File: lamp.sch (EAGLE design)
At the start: 15 parts, among them IC1 LM358D, T2 TIP32C

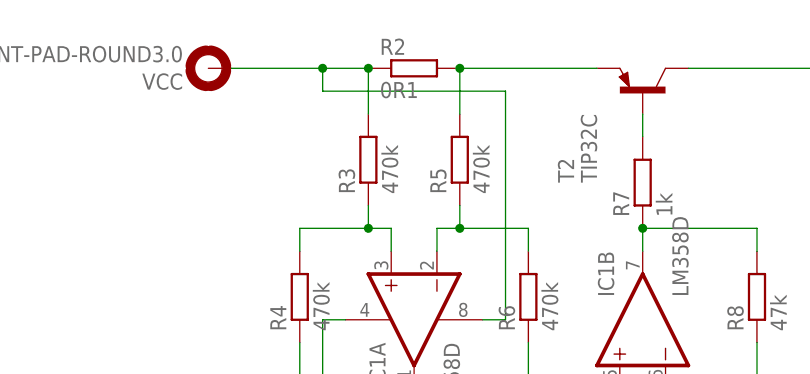
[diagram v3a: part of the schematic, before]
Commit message: Adjusted resistor values & packages.
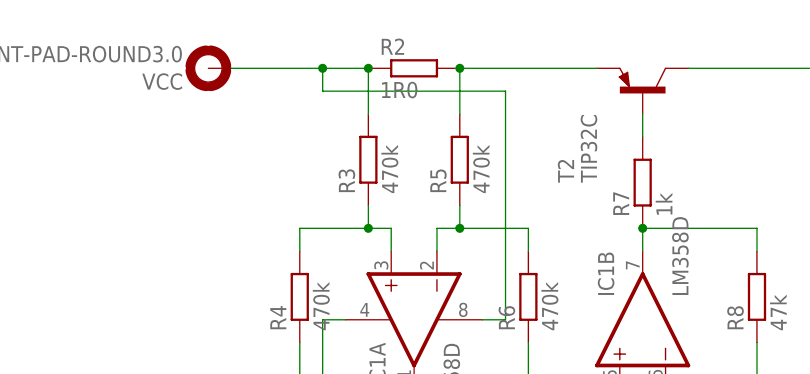
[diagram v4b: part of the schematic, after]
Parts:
- R2: value 0R1 -> 1R0; device resistor:R-EU_0617/17 -> resistor:R-EU_R1210
- R3, R4, R5, R6, R7, R8: device resistor:R-EU_M1206 -> resistor:R-EU_R1206
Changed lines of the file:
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@@
 <part name="IC1" library="linear" deviceset="LM358" device="D" value="LM358D"/>
 <part name="R1" library="pot" deviceset="TRIM_EU-" device="RJ9W" value="10k"/>
-<part name="R2" library="resistor" deviceset="R-EU_" device="0617/17" value="0R1"/>
-<part name="R3" library="resistor" deviceset="R-EU_" device="M1206" value="470k"/>
-<part name="R4" library="resistor" deviceset="R-EU_" device="M1206" value="470k"/>
-<part name="R5" library="resistor" deviceset="R-EU_" device="M1206" value="470k"/>
-<part name="R6" library="resistor" deviceset="R-EU_" device="M1206" value="470k"/>
+<part name="R2" library="resistor" deviceset="R-EU_" device="R1210" value="1R0"/>
+<part name="R3" library="resistor" deviceset="R-EU_" device="R1206" value="470k"/>
+<part name="R4" library="resistor" deviceset="R-EU_" device="R1206" value="470k"/>
+<part name="R5" library="resistor" deviceset="R-EU_" device="R1206" value="470k"/>
+<part name="R6" library="resistor" deviceset="R-EU_" device="R1206" value="470k"/>
 <part name="LED2" library="led" deviceset="Z-POWER-LED" device=""/>
 <part name="LED3" library="led" deviceset="Z-POWER-LED" device=""/>
-<part name="R7" library="resistor" deviceset="R-EU_" device="M1206" value="1k"/>
+<part name="R7" library="resistor" deviceset="R-EU_" device="R1206" value="1k"/>
 <part name="T2" library="transistor" deviceset="TIP32" device="" technology="C"/>
-<part name="R8" library="resistor" deviceset="R-EU_" device="M1206" value="47k"/>
+<part name="R8" library="resistor" deviceset="R-EU_" device="R1206" value="47k"/>
 <part name="VCC" library="holes" deviceset="MOUNT-PAD-ROUND" device="3.0"/>
 <part name="GND" library="holes" deviceset="MOUNT-PAD-ROUND" device="3.0"/>

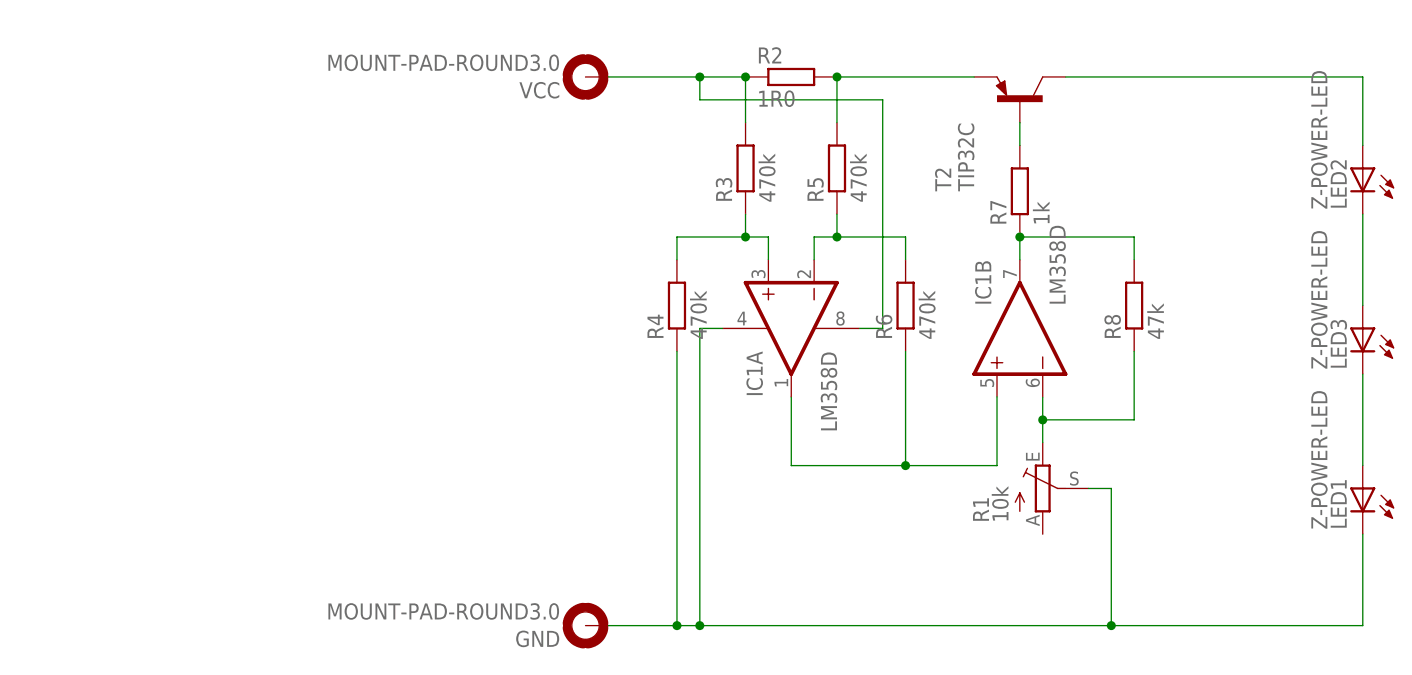
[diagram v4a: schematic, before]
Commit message: Added a power switch.
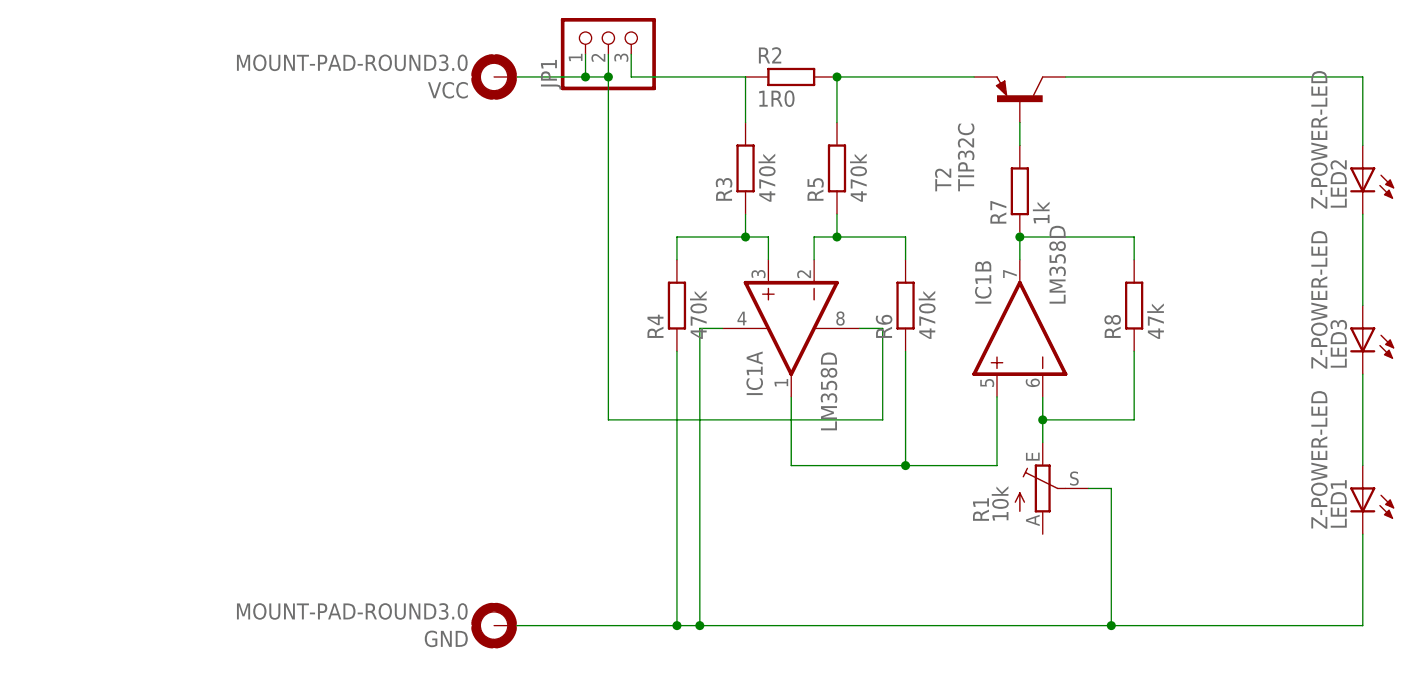
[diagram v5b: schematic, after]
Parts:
- added JP1: (no value), pinhead:PINHD-1X3
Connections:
- new net N$24: JP1.3, R2.1, R3.2
- net VCC: now also JP1.1, JP1.2; no longer R2.1, R3.2
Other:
- moved on the sheet: GND, VCC
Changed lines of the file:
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@@
 <part name="VCC" library="holes" deviceset="MOUNT-PAD-ROUND" device="3.0"/>
 <part name="GND" library="holes" deviceset="MOUNT-PAD-ROUND" device="3.0"/>
+<part name="JP1" library="pinhead" deviceset="PINHD-1X3" device=""/>
 </parts>
 <sheets>
@@
 <instance part="T2" gate="G$1" x="43.18" y="91.44" rot="R90"/>
 <instance part="R8" gate="G$1" x="55.88" y="68.58" rot="R90"/>
-<instance part="VCC" gate="G$1" x="-5.08" y="93.98" rot="R180"/>
-<instance part="GND" gate="G$1" x="-5.08" y="33.02" rot="R180"/>
+<instance part="VCC" gate="G$1" x="-15.24" y="93.98" rot="R180"/>
+<instance part="GND" gate="G$1" x="-15.24" y="33.02" rot="R180"/>
 <instance part="IC1" gate="P" x="17.78" y="66.04" rot="MR90"/>
+<instance part="JP1" gate="A" x="-2.54" y="99.06" rot="R90"/>
 </instances>
 <busses>
 </busses>
 <nets>
-<net name="VCC" class="0">
-<segment>
-<wire x1="-2.54" y1="93.98" x2="7.62" y2="93.98" width="0.1524" layer="91"/>
-<pinref part="R2" gate="G$1" pin="1"/>
-<pinref part="VCC" gate="G$1" pin="MOUNT"/>
-<pinref part="R3" gate="G$1" pin="2"/>
-<wire x1="7.62" y1="93.98" x2="12.7" y2="93.98" width="0.1524" layer="91"/>
-<wire x1="12.7" y1="93.98" x2="12.7" y2="88.9" width="0.1524" layer="91"/>
-<junction x="12.7" y="93.98"/>
-<pinref part="IC1" gate="P" pin="V+"/>
-<wire x1="25.4" y1="66.04" x2="27.94" y2="66.04" width="0.1524" layer="91"/>
-<wire x1="27.94" y1="66.04" x2="27.94" y2="91.44" width="0.1524" layer="91"/>
-<wire x1="27.94" y1="91.44" x2="7.62" y2="91.44" width="0.1524" layer="91"/>
-<wire x1="7.62" y1="91.44" x2="7.62" y2="93.98" width="0.1524" layer="91"/>
-<junction x="7.62" y="93.98"/>
-</segment>
-</net>
 <net name="N$2" class="0">
 <segment>
@@
 <wire x1="53.34" y1="33.02" x2="7.62" y2="33.02" width="0.1524" layer="91"/>
 <wire x1="7.62" y1="33.02" x2="5.08" y2="33.02" width="0.1524" layer="91"/>
-<wire x1="5.08" y1="33.02" x2="-2.54" y2="33.02" width="0.1524" layer="91"/>
+<wire x1="5.08" y1="33.02" x2="-12.7" y2="33.02" width="0.1524" layer="91"/>
 <wire x1="50.8" y1="48.26" x2="53.34" y2="48.26" width="0.1524" layer="91"/>
 <wire x1="53.34" y1="48.26" x2="53.34" y2="33.02" width="0.1524" layer="91"/>
@@
 </segment>
 </net>
+<net name="VCC" class="0">
+<segment>
+<pinref part="JP1" gate="A" pin="1"/>
+<wire x1="-12.7" y1="93.98" x2="-5.08" y2="93.98" width="0.1524" layer="91"/>
+<wire x1="-5.08" y1="96.52" x2="-5.08" y2="93.98" width="0.1524" layer="91"/>
+<pinref part="JP1" gate="A" pin="2"/>
+<wire x1="-5.08" y1="93.98" x2="-2.54" y2="93.98" width="0.1524" layer="91"/>
+<wire x1="-2.54" y1="93.98" x2="-2.54" y2="96.52" width="0.1524" layer="91"/>
+<junction x="-5.08" y="93.98"/>
+<pinref part="VCC" gate="G$1" pin="MOUNT"/>
+<pinref part="IC1" gate="P" pin="V+"/>
+<wire x1="25.4" y1="66.04" x2="27.94" y2="66.04" width="0.1524" layer="91"/>
+<wire x1="27.94" y1="66.04" x2="27.94" y2="55.88" width="0.1524" layer="91"/>
+<wire x1="27.94" y1="55.88" x2="-2.54" y2="55.88" width="0.1524" layer="91"/>
+<wire x1="-2.54" y1="55.88" x2="-2.54" y2="93.98" width="0.1524" layer="91"/>
+<junction x="-2.54" y="93.98"/>
+</segment>
+</net>
+<net name="N$24" class="0">
+<segment>
+<pinref part="R3" gate="G$1" pin="2"/>
+<pinref part="R2" gate="G$1" pin="1"/>
+<wire x1="12.7" y1="93.98" x2="12.7" y2="88.9" width="0.1524" layer="91"/>
+<pinref part="JP1" gate="A" pin="3"/>
+<wire x1="0" y1="96.52" x2="0" y2="93.98" width="0.1524" layer="91"/>
+<wire x1="0" y1="93.98" x2="12.7" y2="93.98" width="0.1524" layer="91"/>
+</segment>
+</net>

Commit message: Added another mounting hole & removed the potentiometer.
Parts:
- removed R1: 10k, pot:TRIM_EU-RJ9W
- added R9: (no value), resistor:R-EU_R1206
- added VCC1: MOUNT-PAD-ROUND3.0, holes:MOUNT-PAD-ROUND3.0
- R8: value 47k -> 470k
- renumbered GND to GROUND
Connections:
- removed net N$24: JP1.3, R2.1, R3.2
- new net N$25: GROUND.MOUNT, JP1.1
- net GND: now also JP1.2, JP1.3, R9.1; no longer GROUND.MOUNT, R1.S
- net N$10: now also R9.2; no longer R1.E
- net VCC: now also R2.1, R3.2, VCC1.MOUNT; no longer JP1.1, JP1.2
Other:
- moved on the sheet: JP1
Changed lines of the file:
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@@
 <part name="LED1" library="led" deviceset="Z-POWER-LED" device=""/>
 <part name="IC1" library="linear" deviceset="LM358" device="D" value="LM358D"/>
-<part name="R1" library="pot" deviceset="TRIM_EU-" device="RJ9W" value="10k"/>
 <part name="R2" library="resistor" deviceset="R-EU_" device="R1210" value="1R0"/>
 <part name="R3" library="resistor" deviceset="R-EU_" device="R1206" value="470k"/>
@@
 <part name="R7" library="resistor" deviceset="R-EU_" device="R1206" value="1k"/>
 <part name="T2" library="transistor" deviceset="TIP32" device="" technology="C"/>
-<part name="R8" library="resistor" deviceset="R-EU_" device="R1206" value="47k"/>
+<part name="R8" library="resistor" deviceset="R-EU_" device="R1206" value="470k"/>
 <part name="VCC" library="holes" deviceset="MOUNT-PAD-ROUND" device="3.0"/>
-<part name="GND" library="holes" deviceset="MOUNT-PAD-ROUND" device="3.0"/>
+<part name="GROUND" library="holes" deviceset="MOUNT-PAD-ROUND" device="3.0"/>
 <part name="JP1" library="pinhead" deviceset="PINHD-1X3" device=""/>
+<part name="R9" library="resistor" deviceset="R-EU_" device="R1206"/>
+<part name="VCC1" library="holes" deviceset="MOUNT-PAD-ROUND" device="3.0"/>
 </parts>
 <sheets>
@@
 <instance part="IC1" gate="A" x="17.78" y="66.04" rot="MR270"/>
 <instance part="IC1" gate="B" x="43.18" y="66.04" rot="R90"/>
-<instance part="R1" gate="1" x="45.72" y="48.26"/>
 <instance part="R2" gate="G$1" x="17.78" y="93.98"/>
 <instance part="R3" gate="G$1" x="12.7" y="83.82" rot="R90"/>
@@
 <instance part="R8" gate="G$1" x="55.88" y="68.58" rot="R90"/>
 <instance part="VCC" gate="G$1" x="-15.24" y="93.98" rot="R180"/>
-<instance part="GND" gate="G$1" x="-15.24" y="33.02" rot="R180"/>
+<instance part="GROUND" gate="G$1" x="-15.24" y="33.02" rot="R180"/>
 <instance part="IC1" gate="P" x="17.78" y="66.04" rot="MR90"/>
-<instance part="JP1" gate="A" x="-2.54" y="99.06" rot="R90"/>
+<instance part="JP1" gate="A" x="-5.08" y="38.1" rot="R90"/>
+<instance part="R9" gate="G$1" x="45.72" y="48.26" rot="R90"/>
+<instance part="VCC1" gate="G$1" x="-15.24" y="63.5" rot="R180"/>
 </instances>
 <busses>
@@
 <pinref part="LED1" gate="G$1" pin="C"/>
 <wire x1="81.28" y1="43.18" x2="81.28" y2="33.02" width="0.1524" layer="91"/>
-<wire x1="81.28" y1="33.02" x2="53.34" y2="33.02" width="0.1524" layer="91"/>
-<pinref part="GND" gate="G$1" pin="MOUNT"/>
-<pinref part="R1" gate="1" pin="S"/>
-<wire x1="53.34" y1="33.02" x2="7.62" y2="33.02" width="0.1524" layer="91"/>
+<wire x1="81.28" y1="33.02" x2="45.72" y2="33.02" width="0.1524" layer="91"/>
+<wire x1="45.72" y1="33.02" x2="7.62" y2="33.02" width="0.1524" layer="91"/>
 <wire x1="7.62" y1="33.02" x2="5.08" y2="33.02" width="0.1524" layer="91"/>
-<wire x1="5.08" y1="33.02" x2="-12.7" y2="33.02" width="0.1524" layer="91"/>
-<wire x1="50.8" y1="48.26" x2="53.34" y2="48.26" width="0.1524" layer="91"/>
-<wire x1="53.34" y1="48.26" x2="53.34" y2="33.02" width="0.1524" layer="91"/>
-<junction x="53.34" y="33.02"/>
 <pinref part="IC1" gate="P" pin="V-"/>
 <wire x1="10.16" y1="66.04" x2="7.62" y2="66.04" width="0.1524" layer="91"/>
@@
 <pinref part="R4" gate="G$1" pin="1"/>
 <wire x1="5.08" y1="63.5" x2="5.08" y2="33.02" width="0.1524" layer="91"/>
+<pinref part="JP1" gate="A" pin="3"/>
+<wire x1="-2.54" y1="35.56" x2="-2.54" y2="33.02" width="0.1524" layer="91"/>
+<wire x1="-2.54" y1="33.02" x2="5.08" y2="33.02" width="0.1524" layer="91"/>
 <junction x="5.08" y="33.02"/>
+<pinref part="JP1" gate="A" pin="2"/>
+<wire x1="-2.54" y1="33.02" x2="-5.08" y2="33.02" width="0.1524" layer="91"/>
+<wire x1="-5.08" y1="33.02" x2="-5.08" y2="35.56" width="0.1524" layer="91"/>
+<junction x="-2.54" y="33.02"/>
+<pinref part="R9" gate="G$1" pin="1"/>
+<wire x1="45.72" y1="43.18" x2="45.72" y2="33.02" width="0.1524" layer="91"/>
+<junction x="45.72" y="33.02"/>
 </segment>
 </net>
@@
 <wire x1="55.88" y1="55.88" x2="45.72" y2="55.88" width="0.1524" layer="91"/>
 <wire x1="45.72" y1="55.88" x2="45.72" y2="58.42" width="0.1524" layer="91"/>
-<pinref part="R1" gate="1" pin="E"/>
 <wire x1="45.72" y1="53.34" x2="45.72" y2="55.88" width="0.1524" layer="91"/>
 <junction x="45.72" y="55.88"/>
+<pinref part="R9" gate="G$1" pin="2"/>
 </segment>
 </net>
@@
 <net name="VCC" class="0">
 <segment>
-<pinref part="JP1" gate="A" pin="1"/>
-<wire x1="-12.7" y1="93.98" x2="-5.08" y2="93.98" width="0.1524" layer="91"/>
-<wire x1="-5.08" y1="96.52" x2="-5.08" y2="93.98" width="0.1524" layer="91"/>
-<pinref part="JP1" gate="A" pin="2"/>
-<wire x1="-5.08" y1="93.98" x2="-2.54" y2="93.98" width="0.1524" layer="91"/>
-<wire x1="-2.54" y1="93.98" x2="-2.54" y2="96.52" width="0.1524" layer="91"/>
-<junction x="-5.08" y="93.98"/>
-<pinref part="VCC" gate="G$1" pin="MOUNT"/>
 <pinref part="IC1" gate="P" pin="V+"/>
 <wire x1="25.4" y1="66.04" x2="27.94" y2="66.04" width="0.1524" layer="91"/>
-<wire x1="27.94" y1="66.04" x2="27.94" y2="55.88" width="0.1524" layer="91"/>
-<wire x1="27.94" y1="55.88" x2="-2.54" y2="55.88" width="0.1524" layer="91"/>
-<wire x1="-2.54" y1="55.88" x2="-2.54" y2="93.98" width="0.1524" layer="91"/>
-<junction x="-2.54" y="93.98"/>
-</segment>
-</net>
-<net name="N$24" class="0">
-<segment>
+<wire x1="27.94" y1="66.04" x2="27.94" y2="91.44" width="0.1524" layer="91"/>
 <pinref part="R3" gate="G$1" pin="2"/>
 <pinref part="R2" gate="G$1" pin="1"/>
 <wire x1="12.7" y1="93.98" x2="12.7" y2="88.9" width="0.1524" layer="91"/>
-<pinref part="JP1" gate="A" pin="3"/>
-<wire x1="0" y1="96.52" x2="0" y2="93.98" width="0.1524" layer="91"/>
-<wire x1="0" y1="93.98" x2="12.7" y2="93.98" width="0.1524" layer="91"/>
-</segment>
-</net>
+<wire x1="-12.7" y1="93.98" x2="-7.62" y2="93.98" width="0.1524" layer="91"/>
+<pinref part="VCC" gate="G$1" pin="MOUNT"/>
+<wire x1="-7.62" y1="93.98" x2="5.08" y2="93.98" width="0.1524" layer="91"/>
+<wire x1="5.08" y1="93.98" x2="12.7" y2="93.98" width="0.1524" layer="91"/>
+<wire x1="27.94" y1="91.44" x2="5.08" y2="91.44" width="0.1524" layer="91"/>
+<wire x1="5.08" y1="91.44" x2="5.08" y2="93.98" width="0.1524" layer="91"/>
+<junction x="5.08" y="93.98"/>
+<pinref part="VCC1" gate="G$1" pin="MOUNT"/>
+<wire x1="-12.7" y1="63.5" x2="-7.62" y2="63.5" width="0.1524" layer="91"/>
+<wire x1="-7.62" y1="63.5" x2="-7.62" y2="93.98" width="0.1524" layer="91"/>
+<junction x="-7.62" y="93.98"/>
+</segment>
+</net>
+<net name="N$25" class="0">
+<segment>
+<pinref part="JP1" gate="A" pin="1"/>
+<wire x1="-12.7" y1="33.02" x2="-7.62" y2="33.02" width="0.1524" layer="91"/>
+<wire x1="-7.62" y1="35.56" x2="-7.62" y2="33.02" width="0.1524" layer="91"/>
+<pinref part="GROUND" gate="G$1" pin="MOUNT"/>
+</segment>
+</net>
